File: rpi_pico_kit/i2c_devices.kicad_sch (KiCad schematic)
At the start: 11 parts, among them J10 OLED Display SSD1306, J11 Conn_01x04_Male, J12 Conn_01x04_Male, U8 AT24CS32

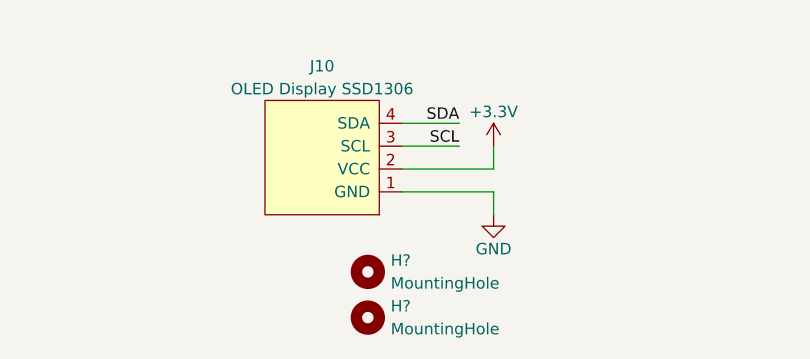
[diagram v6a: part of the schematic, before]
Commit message: added solder jumpers to swd, changed numbering of parts
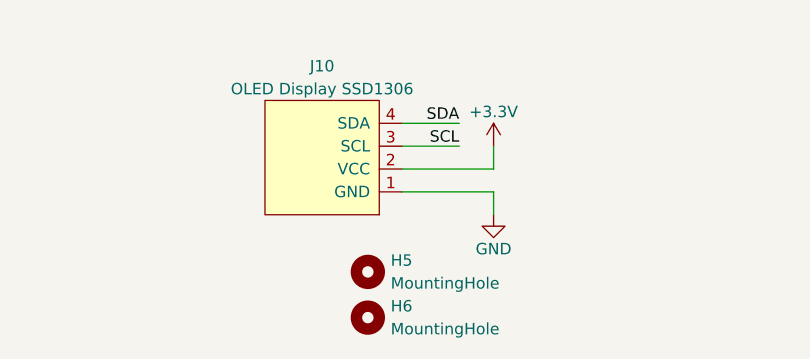
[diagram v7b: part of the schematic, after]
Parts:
- gave numbers to parts that had none: 2
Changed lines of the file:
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@@
   (symbol (lib_id "Mechanical:MountingHole") (at 85.09 128.27 0) (unit 1)
     (in_bom yes) (on_board yes) (fields_autoplaced)
-    (property "Reference" "H?" (id 0) (at 87.63 126.9999 0)
+    (property "Reference" "H6" (id 0) (at 87.63 126.9999 0)
       (effects (font (size 1.27 1.27)) (justify left))
     )
@@
   (symbol (lib_id "power:GND") (at 156.21 116.84 0) (unit 1)
     (in_bom yes) (on_board yes)
-    (property "Reference" "#PWR?" (id 0) (at 156.21 123.19 0)
+    (property "Reference" "#PWR0115" (id 0) (at 156.21 123.19 0)
       (effects (font (size 1.27 1.27)) hide)
     )
@@
   (symbol (lib_id "power:+3.3V") (at 156.21 73.66 0) (unit 1)
     (in_bom yes) (on_board yes)
-    (property "Reference" "#PWR?" (id 0) (at 156.21 77.47 0)
+    (property "Reference" "#PWR0112" (id 0) (at 156.21 77.47 0)
       (effects (font (size 1.27 1.27)) hide)
     )
@@
   (symbol (lib_id "power:GND") (at 156.21 86.36 0) (unit 1)
     (in_bom yes) (on_board yes)
-    (property "Reference" "#PWR?" (id 0) (at 156.21 92.71 0)
+    (property "Reference" "#PWR0113" (id 0) (at 156.21 92.71 0)
       (effects (font (size 1.27 1.27)) hide)
     )
@@
   (symbol (lib_id "power:GND") (at 99.06 116.84 0) (unit 1)
     (in_bom yes) (on_board yes)
-    (property "Reference" "#PWR?" (id 0) (at 99.06 123.19 0)
+    (property "Reference" "#PWR0111" (id 0) (at 99.06 123.19 0)
       (effects (font (size 1.27 1.27)) hide)
     )
@@
   (symbol (lib_id "power:GND") (at 222.25 104.14 0) (unit 1)
     (in_bom yes) (on_board yes)
-    (property "Reference" "#PWR?" (id 0) (at 222.25 110.49 0)
+    (property "Reference" "#PWR0119" (id 0) (at 222.25 110.49 0)
       (effects (font (size 1.27 1.27)) hide)
     )
@@
   (symbol (lib_id "power:+5V") (at 46.99 66.04 0) (unit 1)
     (in_bom yes) (on_board yes)
-    (property "Reference" "#PWR?" (id 0) (at 46.99 69.85 0)
+    (property "Reference" "#PWR0106" (id 0) (at 46.99 69.85 0)
       (effects (font (size 1.27 1.27)) hide)
     )
@@
   (symbol (lib_id "power:+3.3V") (at 85.09 66.04 0) (unit 1)
     (in_bom yes) (on_board yes)
-    (property "Reference" "#PWR?" (id 0) (at 85.09 69.85 0)
+    (property "Reference" "#PWR0108" (id 0) (at 85.09 69.85 0)
       (effects (font (size 1.27 1.27)) hide)
     )
@@
   (symbol (lib_id "power:+3.3V") (at 93.98 66.04 0) (unit 1)
     (in_bom yes) (on_board yes)
-    (property "Reference" "#PWR?" (id 0) (at 93.98 69.85 0)
+    (property "Reference" "#PWR0109" (id 0) (at 93.98 69.85 0)
       (effects (font (size 1.27 1.27)) hide)
     )
@@
   (symbol (lib_id "power:+5V") (at 55.88 66.04 0) (unit 1)
     (in_bom yes) (on_board yes)
-    (property "Reference" "#PWR?" (id 0) (at 55.88 69.85 0)
+    (property "Reference" "#PWR0107" (id 0) (at 55.88 69.85 0)
       (effects (font (size 1.27 1.27)) hide)
     )
@@
   (symbol (lib_id "power:+3.3V") (at 99.06 109.22 0) (unit 1)
     (in_bom yes) (on_board yes)
-    (property "Reference" "#PWR?" (id 0) (at 99.06 113.03 0)
+    (property "Reference" "#PWR0110" (id 0) (at 99.06 113.03 0)
       (effects (font (size 1.27 1.27)) hide)
     )
@@
   (symbol (lib_id "power:GND") (at 209.55 107.95 0) (unit 1)
     (in_bom yes) (on_board yes)
-    (property "Reference" "#PWR?" (id 0) (at 209.55 114.3 0)
+    (property "Reference" "#PWR0118" (id 0) (at 209.55 114.3 0)
       (effects (font (size 1.27 1.27)) hide)
     )
@@
   (symbol (lib_id "power:+5V") (at 156.21 104.14 0) (unit 1)
     (in_bom yes) (on_board yes)
-    (property "Reference" "#PWR?" (id 0) (at 156.21 107.95 0)
+    (property "Reference" "#PWR0114" (id 0) (at 156.21 107.95 0)
       (effects (font (size 1.27 1.27)) hide)
     )
@@
   (symbol (lib_id "power:GND") (at 196.85 104.14 0) (unit 1)
     (in_bom yes) (on_board yes)
-    (property "Reference" "#PWR?" (id 0) (at 196.85 110.49 0)
+    (property "Reference" "#PWR0116" (id 0) (at 196.85 110.49 0)
       (effects (font (size 1.27 1.27)) hide)
     )
@@
   (symbol (lib_id "power:+3.3V") (at 209.55 81.28 0) (unit 1)
     (in_bom yes) (on_board yes)
-    (property "Reference" "#PWR?" (id 0) (at 209.55 85.09 0)
+    (property "Reference" "#PWR0117" (id 0) (at 209.55 85.09 0)
       (effects (font (size 1.27 1.27)) hide)
     )
@@
   (symbol (lib_id "power:GND") (at 223.52 88.9 0) (unit 1)
     (in_bom yes) (on_board yes)
-    (property "Reference" "#PWR?" (id 0) (at 223.52 95.25 0)
+    (property "Reference" "#PWR0120" (id 0) (at 223.52 95.25 0)
       (effects (font (size 1.27 1.27)) hide)
     )
@@
   (symbol (lib_id "Mechanical:MountingHole") (at 85.09 123.19 0) (unit 1)
     (in_bom yes) (on_board yes) (fields_autoplaced)
-    (property "Reference" "H?" (id 0) (at 87.63 121.9199 0)
-      (effects (font (size 1.27 1.27)) (justify left))
-    )
+    (property "Reference" "H5" (id 0) (at 87.63 121.9199 0)
+      (effects (font (size 1.27 1.27)) (justify left))
+    )
